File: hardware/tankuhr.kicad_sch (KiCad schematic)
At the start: 29 parts, among them J1 Conn_01x04_Pin, J2 Conn_01x04_Pin, J3 Conn_01x04_Pin, U1 TBA1-1211, U2 XIAO-ESP32-C3-SMD

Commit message: start with r2 hardware
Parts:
- added D2: 1N5817, Diode_THT:D_DO-41_SOD81_P7.62mm_Horizontal, symbol Device:D_Schottky
- added D3: LED, LED_SMD:LED_PLCC-2_3.4x3.0mm_AK, symbol Device:LED
- added F1: 1A, Fuse:Fuse_1206_3216Metric, symbol Device:Fuse
- added JP1: SolderJumper_2_Bridged, Jumper:SolderJumper-2_P1.3mm_Bridged2Bar_Pad1.0x1.5mm, symbol Jumper:SolderJumper_2_Bridged
- C3, C4, C5, C6, R6, R7: footprint Capacitor_SMD:C_0805_2012Metric -> Capacitor_SMD:C_0805_2012Metric_Pad1.18x1.45mm_HandSolder
- J1, J2, J3: footprint Connector_PinHeader_2.54mm:PinHeader_1x04_P2.54mm_Vertical -> Connector_JST:JST_GH_BM04B-GHS-TBT_1x04-1MP_P1.25mm_Vertical
- R1, R2, R3, R5: footprint Resistor_SMD:R_0805_2012Metric -> Resistor_SMD:R_0805_2012Metric_Pad1.20x1.40mm_HandSolder
- R4: value 0 -> ?; footprint Connector_PinHeader_2.54mm:PinHeader_1x02_P2.54mm_Vertical -> Resistor_SMD:R_0805_2012Metric_Pad1.20x1.40mm_HandSolder
- TP1, TP2, TP3, TP4: footprint TestPoint:TestPoint_THTPad_2.0x2.0mm_Drill1.0mm -> TestPoint:TestPoint_Pad_D1.0mm
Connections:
- net +12V: now also D2.1 (K); no longer J1.1 (Pin_1), J1.2 (Pin_2)
- net GND: now also D3.1 (K), JP1.2 (B); no longer R4.2
- net GNDA: now also J1.1 (Pin_1), J1.2 (Pin_2); no longer J1.3 (Pin_3), J1.4 (Pin_4)
- net SENSOR_FUEL_FLOW: now also J2.1 (Pin_1); no longer J2.4 (Pin_4)
- net SENSOR_FUEL_LEVEL: now also J2.4 (Pin_4); no longer J2.1 (Pin_1)
- net at C2.2, C3.2, L2.2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: now also JP1.1 (A); no longer R4.1
- net USER_LED0: now reaches U2.4 (GPIO5_A3_D3)
- net USER_LED0: now also R4.1
- new net: D3.2 (A), R4.2
- new net: D2.2 (A), F1.2
- new net: F1.1, J1.3 (Pin_3), J1.4 (Pin_4)
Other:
- note added: "TODO für r2: ESD-Schutz?"
- note removed: "TODO für r2: Verpolschutz (Diode), ESD-Schutz?, Stecker, Fuse, bessere Lötbrücke"
- moved on the sheet: J1

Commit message: WIP
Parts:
- removed C1: 22u / 10V, Capacitor_THT:CP_Radial_D4.0mm_P1.50mm, symbol Device:C_Polarized
- removed C3: 100n / >35V, Capacitor_SMD:C_0805_2012Metric_Pad1.18x1.45mm_HandSolder, symbol Device:C
- removed D1, D3: LED, LED_SMD:LED_PLCC-2_3.4x3.0mm_AK, symbol Device:LED
- removed D2: 1N5817, Diode_THT:D_DO-41_SOD81_P7.62mm_Horizontal, symbol Device:D_Schottky
- removed L2: 2uH, Inductor_THT:L_Axial_L7.0mm_D3.3mm_P10.16mm_Horizontal_Fastron_MICC, symbol Device:L
- removed R3: 390, Resistor_SMD:R_0805_2012Metric_Pad1.20x1.40mm_HandSolder, symbol Device:R
- removed R4: ?, Resistor_SMD:R_0805_2012Metric_Pad1.20x1.40mm_HandSolder, symbol Device:R
- removed U1: TBA1-1211, Converter_DCDC:Converter_DCDC_TRACO_TBA1-xxxx_THT, symbol Converter_DCDC:TBA1-1211
- added C1: 1n, Capacitor_SMD:C_0805_2012Metric_Pad1.18x1.45mm_HandSolder, symbol Device:C
- added C3: 10u, Capacitor_THT:CP_Radial_D5.0mm_P2.00mm, symbol Device:C_Polarized
- added D1: BAT54W, Package_TO_SOT_SMD:SOT-323_SC-70, symbol Diode:BAT54W
- added R10: 220, Resistor_SMD:R_0805_2012Metric_Pad1.20x1.40mm_HandSolder, symbol Device:R
- added R11: 0, Resistor_SMD:R_0805_2012Metric_Pad1.20x1.40mm_HandSolder, symbol Device:R
- added R8: 4.7k, Resistor_SMD:R_0805_2012Metric_Pad1.20x1.40mm_HandSolder, symbol Device:R
- added R9: 100, Resistor_SMD:R_0805_2012Metric_Pad1.20x1.40mm_HandSolder, symbol Device:R
- added U1: R-78E5.0-0.5, Converter_DCDC:Converter_DCDC_RECOM_R-78E-0.5_THT, symbol Regulator_Switching:R-78E5.0-0.5
- added U3: MCP6002-xMC, Package_DFN_QFN:DFN-8-1EP_3x2mm_P0.5mm_EP1.75x1.45mm, symbol Amplifier_Operational:MCP6002-xMC
- C2: value 100u / 35V -> 4.7u; footprint Capacitor_THT:CP_Radial_D8.0mm_P3.50mm -> Capacitor_THT:CP_Radial_D5.0mm_P2.00mm
- C5: value 100n -> 1n
- L1: value 2uH -> L; footprint Inductor_THT:L_Axial_L7.0mm_D3.3mm_P10.16mm_Horizontal_Fastron_MICC -> asdf:RECOM RLS-126
- R1: value 220 -> 3.3k / 330
- R2: value 6.8k -> 1k
- R5: value 330 -> 220
- R6, R7: footprint Capacitor_SMD:C_0805_2012Metric_Pad1.18x1.45mm_HandSolder -> Resistor_SMD:R_0805_2012Metric_Pad1.20x1.40mm_HandSolder
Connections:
- net +12V: now also C3.1, D1.3 (K)
- net +3.3V: now also J3.2 (Pin_2), R1.2, R8.1
- net +5V: now also U1.3 (OUT); no longer R1.2
- net GND: now also C1.2, R9.1; no longer J3.2 (Pin_2)
- net GNDA: now also C2.2, JP1.1 (A), C3.2, U1.2 (GND)
- net SENSOR_FUEL_FLOW: now also R8.2
- net SENSOR_FUEL_LEVEL: now also R11.1, U3.3 (+); no longer R2.1
- net at C2.1, L1.2: now also U1.1 (IN)
- net SDA: now reaches J3.1 (Pin_1), R6.2, U2.5 (GPIO6_D4_SDA)
- net at R2.2: now also R9.2, U3.2 (-); no longer U2.1 (GPIO2_A0_D0)
- net D1: now reaches C5.1, R5.2, U2.2 (GPIO3_A1_D1)
- net SCL: now reaches J3.4 (Pin_4), R7.2, U2.6 (GPIO7_D5_SCL)
- net at F1.2: now also D1.1 (A)
- net USER_LED0: no longer names the net of U2.4 (GPIO5_A3_D3)
- new net: R10.1, R11.2, R2.1, U3.1
- new net D0: C1.1, R10.2, U2.1 (GPIO2_A0_D0)
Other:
- moved on the sheet: C4, C5, C6, F1, J1, J3, JP1, R1, R5, R6, R7, U2

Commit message: complete r2 hardware
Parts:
- removed U3: MCP6002-xMC, Package_DFN_QFN:DFN-8-1EP_3x2mm_P0.5mm_EP1.75x1.45mm, symbol Amplifier_Operational:MCP6002-xMC
- added D2, D3, D4: LED, LED_SMD:LED_0805_2012Metric_Pad1.15x1.40mm_HandSolder, symbol Device:LED
- added J4: Micro_SD_Card_Det1, Connector_Card:microSD_HC_Molex_104031-0811, symbol Connector:Micro_SD_Card_Det1
- added R12, R3, R4: 150, Resistor_SMD:R_0805_2012Metric_Pad1.20x1.40mm_HandSolder, symbol Device:R
- added U5: MCP6001-OT, Package_TO_SOT_SMD:SOT-23-5, symbol Amplifier_Operational:MCP6001-OT
- L1: footprint asdf:RECOM RLS-126 -> Library:RECOM RLS-120
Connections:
- net +3.3V: now also D2.2 (A), J4.4 (VDD), U5.5 (V+)
- net GND: now also J4.10 (SHIELD), J4.6 (VSS), R12.2, R3.2, R4.2, U5.2 (V-)
- net SENSOR_FUEL_LEVEL: now also U5.3 (+)
- net at R10.1, R11.2, R2.1: now also U5.1
- net at R2.2, R9.2: now also U5.4 (-)
- net SD_MISO: now reaches U2.10 (GPIO9_D9_MISO)
- net SD_MISO: now also J4.7 (DAT0)
- net SD_MOSI: now reaches U2.11 (GPIO10_D10_MOSI)
- net SD_MOSI: now also J4.3 (CMD)
- net LED_0: now reaches U2.4 (GPIO5_A3_D3)
- net LED_0: now also D3.2 (A)
- net LED_1: now reaches U2.7 (GPIO21_D6_TX)
- net LED_1: now also D4.2 (A)
- net SD_CS: now reaches U2.8 (GPIO20_D7_RX)
- net SD_CS: now also J4.2 (DAT3/CD)
- net SD_CLK: now reaches U2.9 (GPIO8_D8_SCK)
- net SD_CLK: now also J4.5 (CLK)
- new net: D3.1 (K), R4.1
- new net: D2.1 (K), R3.1
- new net: D4.1 (K), R12.1
- no-connect marks 0 -> 10
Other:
- moved on the sheet: C4, C6

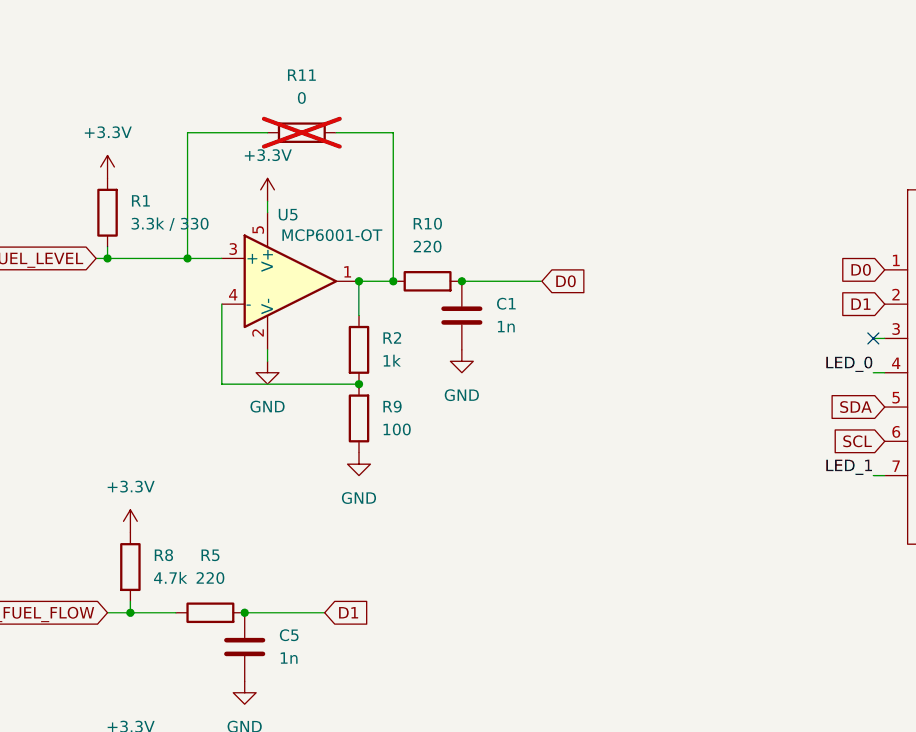
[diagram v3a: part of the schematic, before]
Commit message: hardware: new filter design
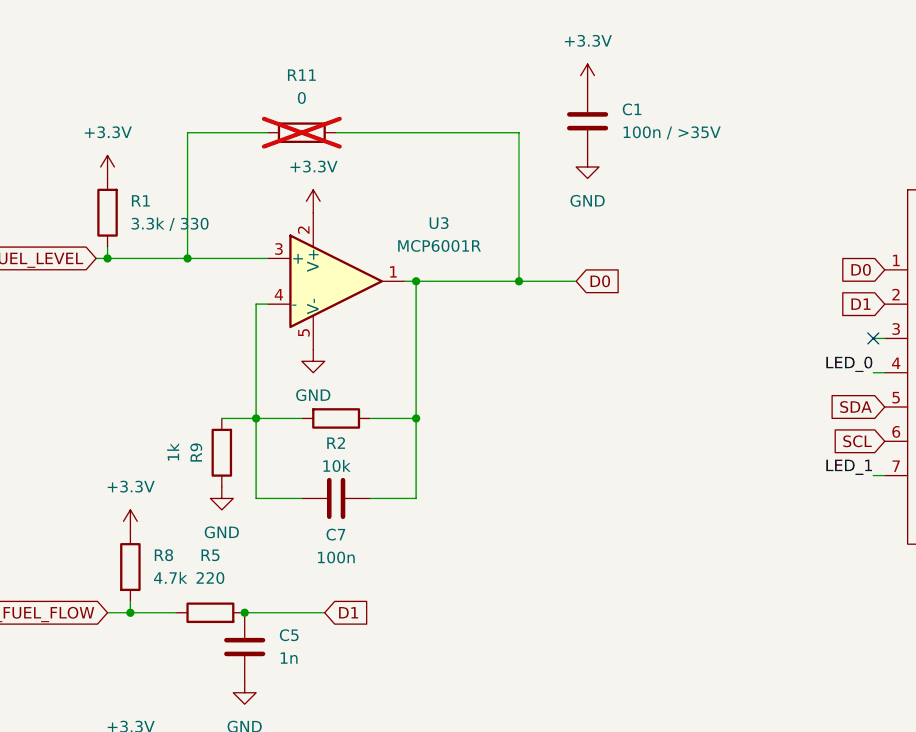
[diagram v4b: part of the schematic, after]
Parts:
- removed R10: 220, Resistor_SMD:R_0805_2012Metric_Pad1.20x1.40mm_HandSolder, symbol Device:R
- removed U5: MCP6001-OT, Package_TO_SOT_SMD:SOT-23-5, symbol Amplifier_Operational:MCP6001-OT
- added C7: 100n, Capacitor_SMD:C_0805_2012Metric_Pad1.18x1.45mm_HandSolder, symbol Device:C
- added U3: MCP6001R, Package_TO_SOT_SMD:SOT-23-5, symbol Amplifier_Operational:MCP6001R
- C1: value 1n -> 100n / >35V
- H1, H2, H3, H4: footprint MountingHole:MountingHole_2.2mm_M2 -> MountingHole:MountingHole_3.2mm_M3
- R2: value 1k -> 10k
- R9: value 100 -> 1k
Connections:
- net +3.3V: now also C1.1, U3.2 (V+)
- net D0: now also R11.2, R2.1, C7.2, U3.1; no longer C1.1
- net GND: now also U3.5 (V-)
- net SENSOR_FUEL_LEVEL: now also U3.3 (+)
- net at R2.2, R9.2: now also C7.1, U3.4 (-)

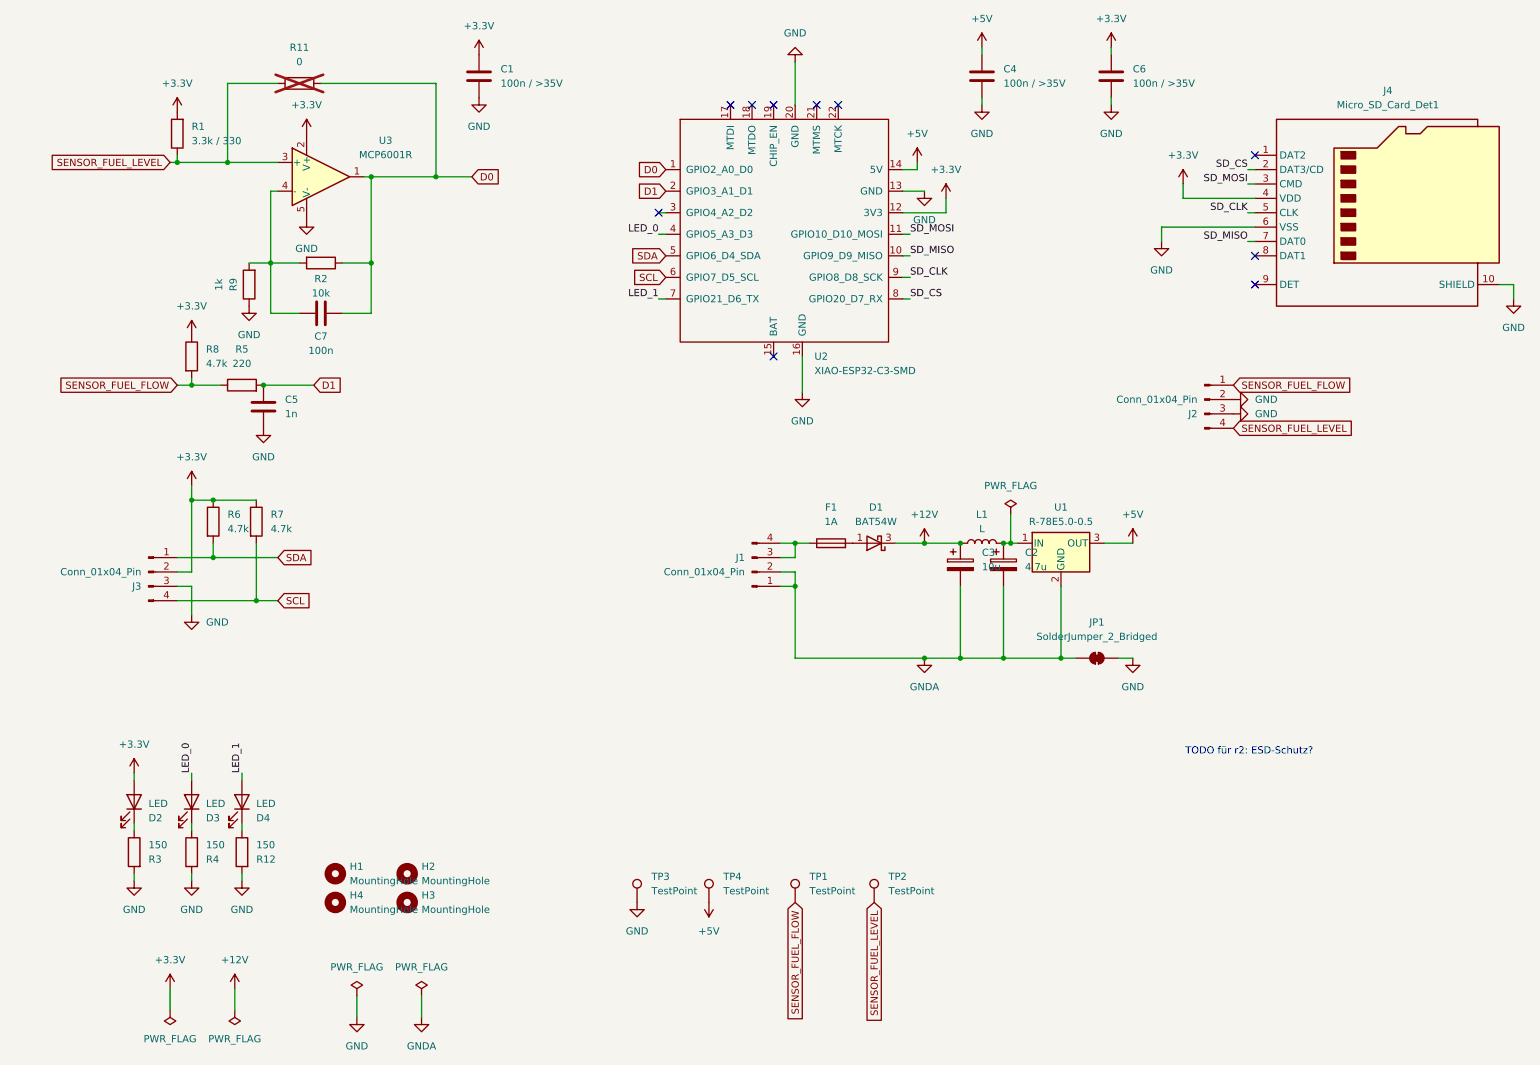
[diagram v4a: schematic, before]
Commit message: hardware: start BOM in kicad
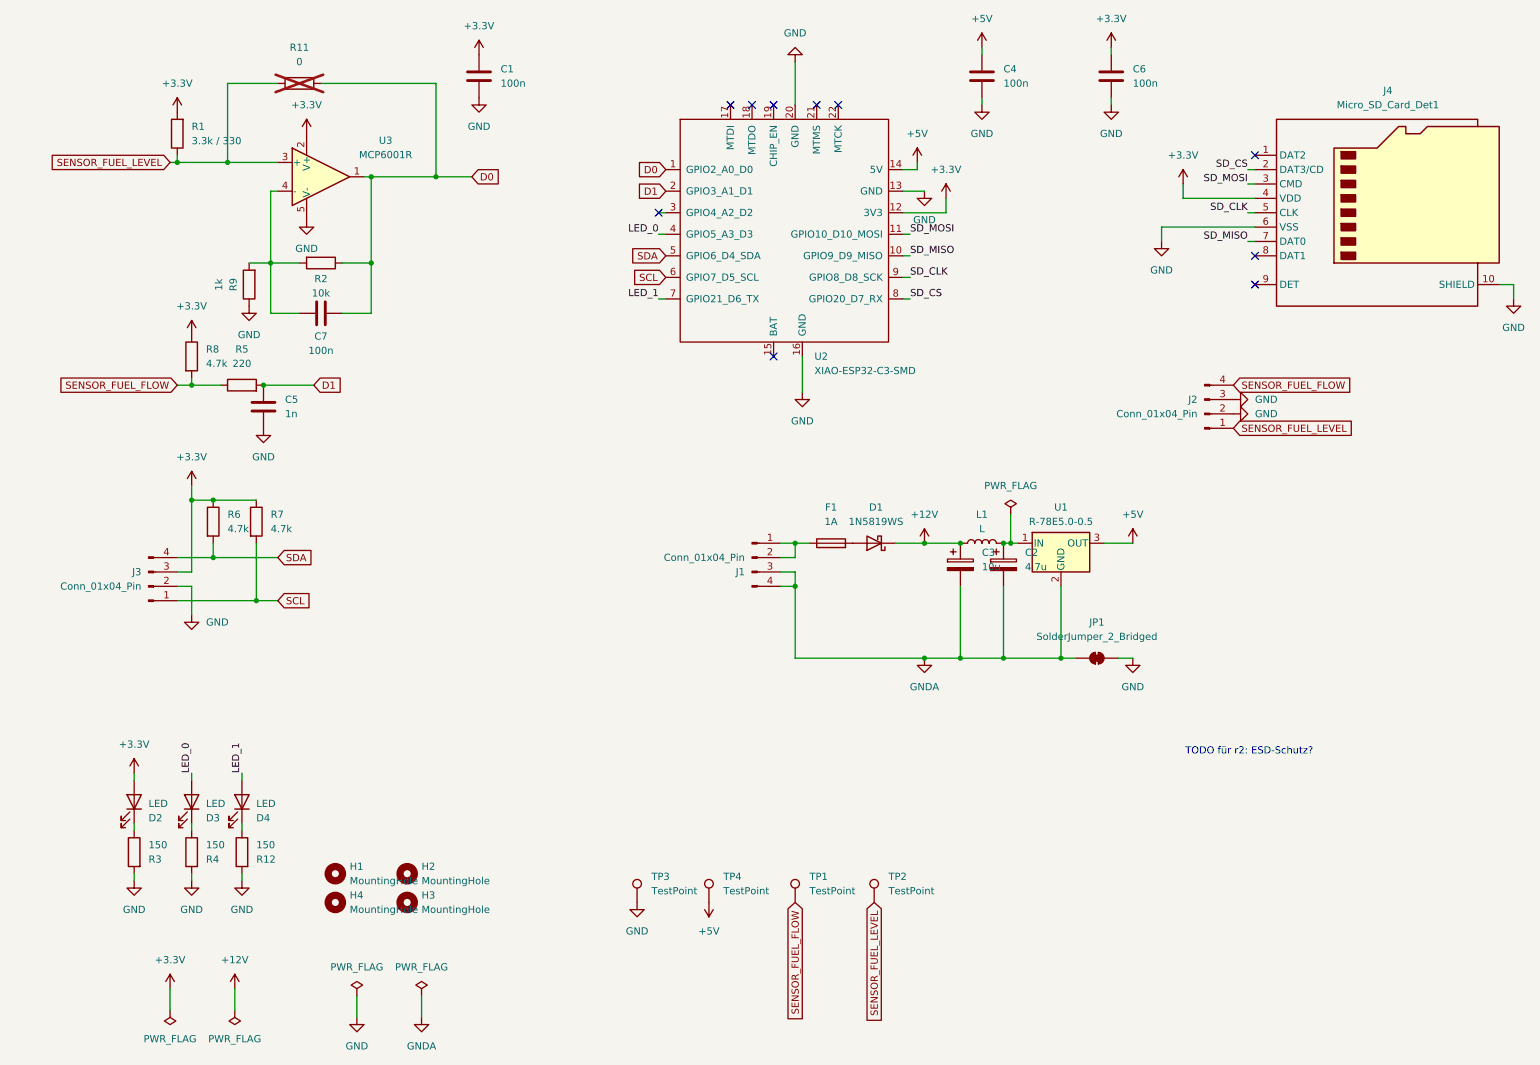
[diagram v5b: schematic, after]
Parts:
- removed D1: BAT54W, Package_TO_SOT_SMD:SOT-323_SC-70, symbol Diode:BAT54W
- added D1: 1N5819WS, Diode_SMD:D_SOD-323, symbol Diode:1N5819WS
- C1, C4, C6: value 100n / >35V -> 100n; Reichelt Nr (none) -> KEM X7R0805 100N
- C2: Reichelt Nr (none) -> M-A 4,7U 50
- C3: Reichelt Nr (none) -> M-A 10U 50
- C5: Reichelt Nr (none) -> KEM X7R0805 1,0N
- C7: Reichelt Nr (none) -> KEM X7R0805 100N
- D2, D3, D4: Reichelt Nr (none) -> EVL 17-21SYGC
- F1: Reichelt Nr (none) -> PTC FSMD1001206R
- J1, J2, J3: footprint Connector_JST:JST_GH_BM04B-GHS-TBT_1x04-1MP_P1.25mm_Vertical -> Connector_Molex:Molex_PicoBlade_53398-0471_1x04-1MP_P1.25mm_Vertical; Reichelt Nr (none) -> MOLEX 533980471
- R1: Reichelt Nr (none) -> SMD-0805 3,30K
- R12, R3, R4: Reichelt Nr (none) -> SMD-0805 150
- R2: Reichelt Nr (none) -> SMD-0805 10,0K
- R5: Reichelt Nr (none) -> SMD-0805 220
- R6, R7, R8: Reichelt Nr (none) -> SMD-0805 4,70K
- R9: Reichelt Nr (none) -> SMD-0805 1,00K
- U1: Reichelt Nr (none) -> R-78E50-05
- U2: Reichelt Nr (none) -> XIAO ESP32C6
- U3: Reichelt Nr (none) -> MCP6001T-I/OT
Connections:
- net +12V: now also D1.1 (K)
- net +3.3V: now also J3.3 (Pin_3); no longer J3.2 (Pin_2)
- net GND: now also J3.2 (Pin_2); no longer J3.3 (Pin_3)
- net GNDA: now also J1.3 (Pin_3), J1.4 (Pin_4); no longer J1.1 (Pin_1), J1.2 (Pin_2)
- net SCL: now also J3.1 (Pin_1); no longer J3.4 (Pin_4)
- net SDA: now also J3.4 (Pin_4); no longer J3.1 (Pin_1)
- net SENSOR_FUEL_FLOW: now also J2.4 (Pin_4); no longer J2.1 (Pin_1)
- net SENSOR_FUEL_LEVEL: now also J2.1 (Pin_1); no longer J2.4 (Pin_4)
- net at F1.2: now also D1.2 (A)
- new net: F1.1, J1.1 (Pin_1), J1.2 (Pin_2)

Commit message: add LCSC BOM
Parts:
- C1, C4, C6, C7: LCSC Nr (none) -> C49678
- C2: LCSC Nr (none) -> C178709
- C3: LCSC Nr (none) -> C713348
- C5: LCSC Nr (none) -> C94121
- D1: LCSC Nr (none) -> C191023
- D2, D3, D4: LCSC Nr (none) -> C919444
- F1: LCSC Nr (none) -> C7542957
- J1, J2, J3: LCSC Nr (none) -> C17617036
- J4: LCSC Nr (none) -> C585350
- R1: LCSC Nr (none) -> C114531
- R12, R3, R4: LCSC Nr (none) -> C856688
- R2: LCSC Nr (none) -> C84376
- R5: LCSC Nr (none) -> C865304
- R6, R7, R8: LCSC Nr (none) -> C60816
- R9: LCSC Nr (none) -> C95781
- U1: LCSC Nr (none) -> C18212367
- U3: LCSC Nr (none) -> C116490
